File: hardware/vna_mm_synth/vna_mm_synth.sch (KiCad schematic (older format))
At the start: 0 parts

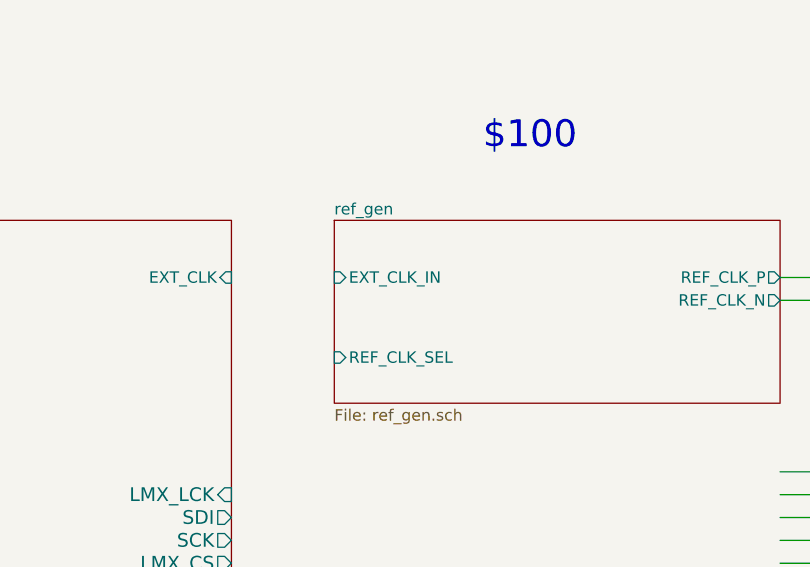
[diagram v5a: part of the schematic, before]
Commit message: component placement on vna ref board
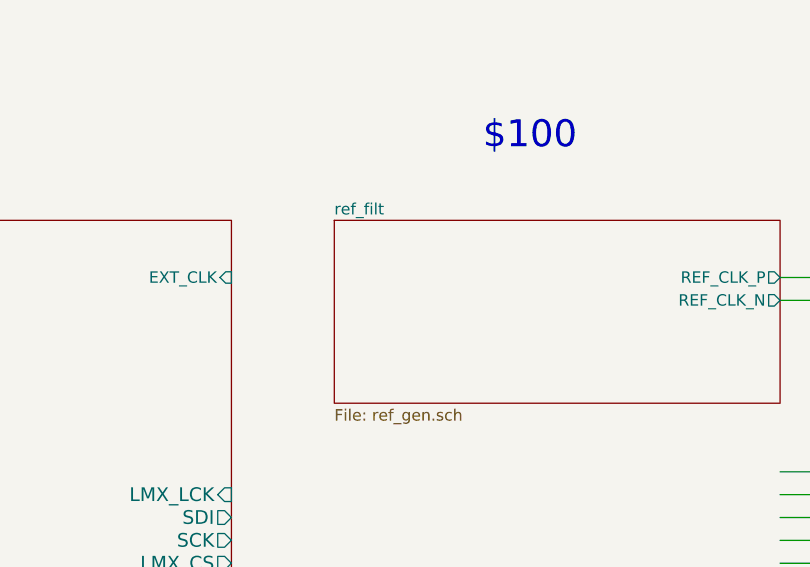
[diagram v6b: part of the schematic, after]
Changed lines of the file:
@@
 S 4300 2950 1950 800
 U 5DB13A27
-F0 "ref_gen" 50
+F0 "ref_filt" 50
 F1 "ref_gen.sch" 50
 F2 "REF_CLK_P" O R 6250 3200 50
 F3 "REF_CLK_N" O R 6250 3300 50
-F4 "EXT_CLK_IN" I L 4300 3200 50
-F5 "REF_CLK_SEL" I L 4300 3550 50
 $EndSheet
 Wire Wire Line

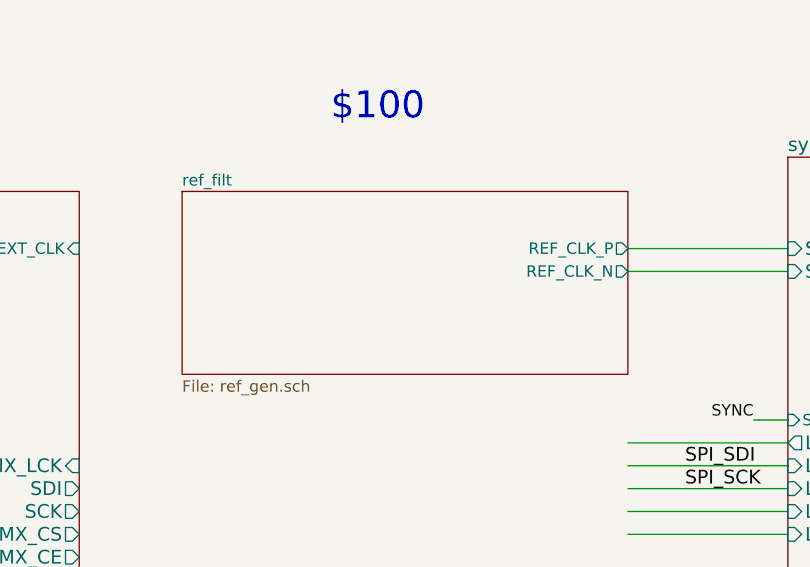
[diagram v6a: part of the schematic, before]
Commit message: cleanup and update vna mm synth schematic for modern kicad libraries
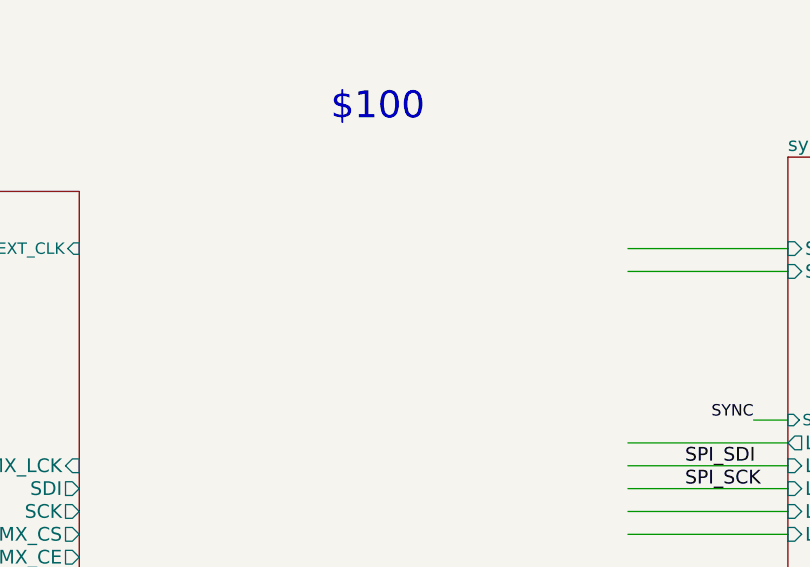
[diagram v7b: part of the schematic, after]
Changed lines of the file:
@@
 $Descr C 22000 17000
 encoding utf-8
-Sheet 1 12
+Sheet 1 11
 Title ""
 Date ""
@@
 Text Label 7900 6300 2    50   ~ 0
 VTUNE_TLM
-$Sheet
-S 4300 2950 1950 800
-U 5DB13A27
-F0 "ref_filt" 50
-F1 "ref_gen.sch" 50
-F2 "REF_CLK_P" O R 6250 3200 50
-F3 "REF_CLK_N" O R 6250 3300 50
-$EndSheet
 Wire Wire Line
 	12500 10300 12750 10300

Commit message: footprint assignment
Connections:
- net labels added: FILT_~SYNC
- net labels removed: FILT_~LDAC
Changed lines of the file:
@@
 F10 "VC_A_EN" I L 10750 9850 50
 F11 "FILT_VTUNE" O R 12500 10300 50
-F12 "FILT_SEN" I L 10750 10300 50
+F12 "FILT_~SYNC" I L 10750 10300 50
 $EndSheet
 Wire Wire Line
@@
 	10750 10300 10600 10300
 Text Label 10600 10300 2    50   ~ 0
-FILT_~LDAC
-Text Label 7900 7200 2    50   ~ 0
-FILT_~LDAC
+FILT_~SYNC
 Text Label 6800 3950 2    50   ~ 0
 SYNC
 Wire Wire Line
 	6800 3950 6950 3950
+Text Label 7900 5250 2    50   ~ 0
+FILT_~SYNC
 $EndSCHEMATC
